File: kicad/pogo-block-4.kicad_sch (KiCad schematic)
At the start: 28 parts, among them J26 VCA_IN, U4 THAT2180, U5 THAT2180, U6 TL072, U63 TL072

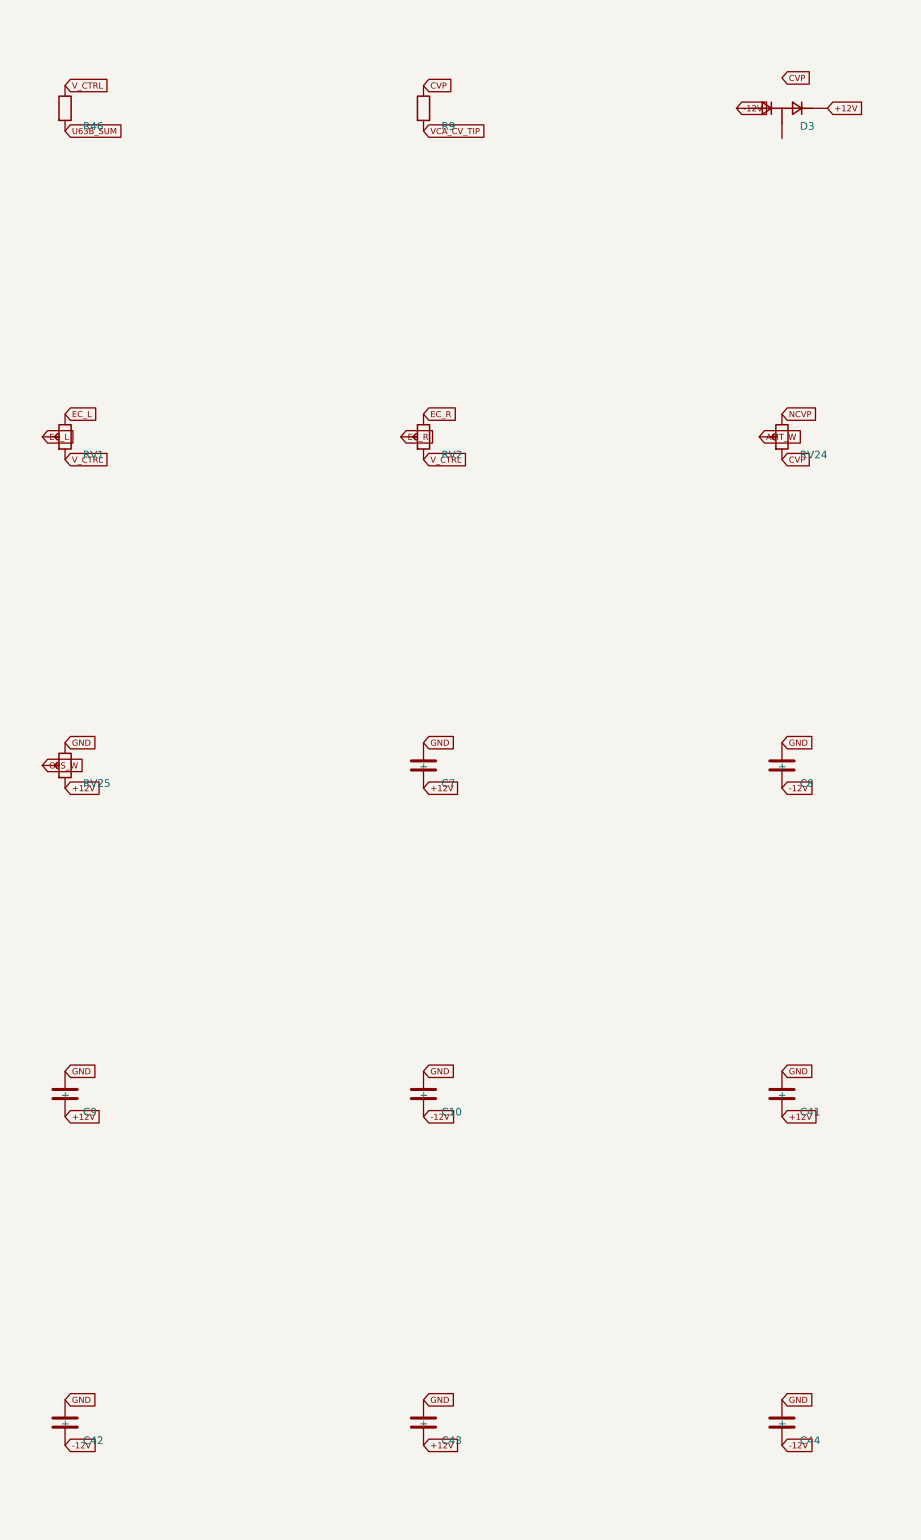
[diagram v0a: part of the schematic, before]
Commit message: 0015-component-audit: apply component verification fixes
Board-breaking:
- that2180: real MPN THAT2180AL08-U (grade A) + package SIP-8 (THT); vendor
  Package_SIP/SIP-8_2.54mm footprint; fix components.yaml U4/U5 + CLAUDE.md.
  The 2180 has no SMD/SOIC variant.
- bat54s: redraw symbol to real series topology (1=A1, 2=K2, 3=K1;A2 junction);
  swap pins 2<->3 on all 24 BAT54S instances (blocks A/1/3/4) so signal sits on the
  junction (pin3), +12V on K2 (pin2), -12V on A1 (pin1); fix aux-cv-protection.md +
  block-A spec (both mislabeled the signal node as pin 2).

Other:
- R_INV_IN/R_INV_FB: add tol 1% (header-required >60 dB null).
- slide_pot_45mm: MPN RA4522F (Alpha 45mm, Rapid/Banzai); fix datasheet link.
- bzx84c10: add shared BZX84_SER datasheet (committed PDF + sha256); canonical MPN.
- opa1612: add symbol opamp2. bourns_3296w/3224w: fix version strings.
- cd4053 symbol doc# -> SCHS047O; c.yaml pin1 '+' -> '~' (non-polarized).

Jack S/T/TN reconciliation deferred (its own change). Plugin DSP untouched.
Regenerated all schematics, BOM, fp-lib-table, footprint SVGs, panel; 5 gates green.
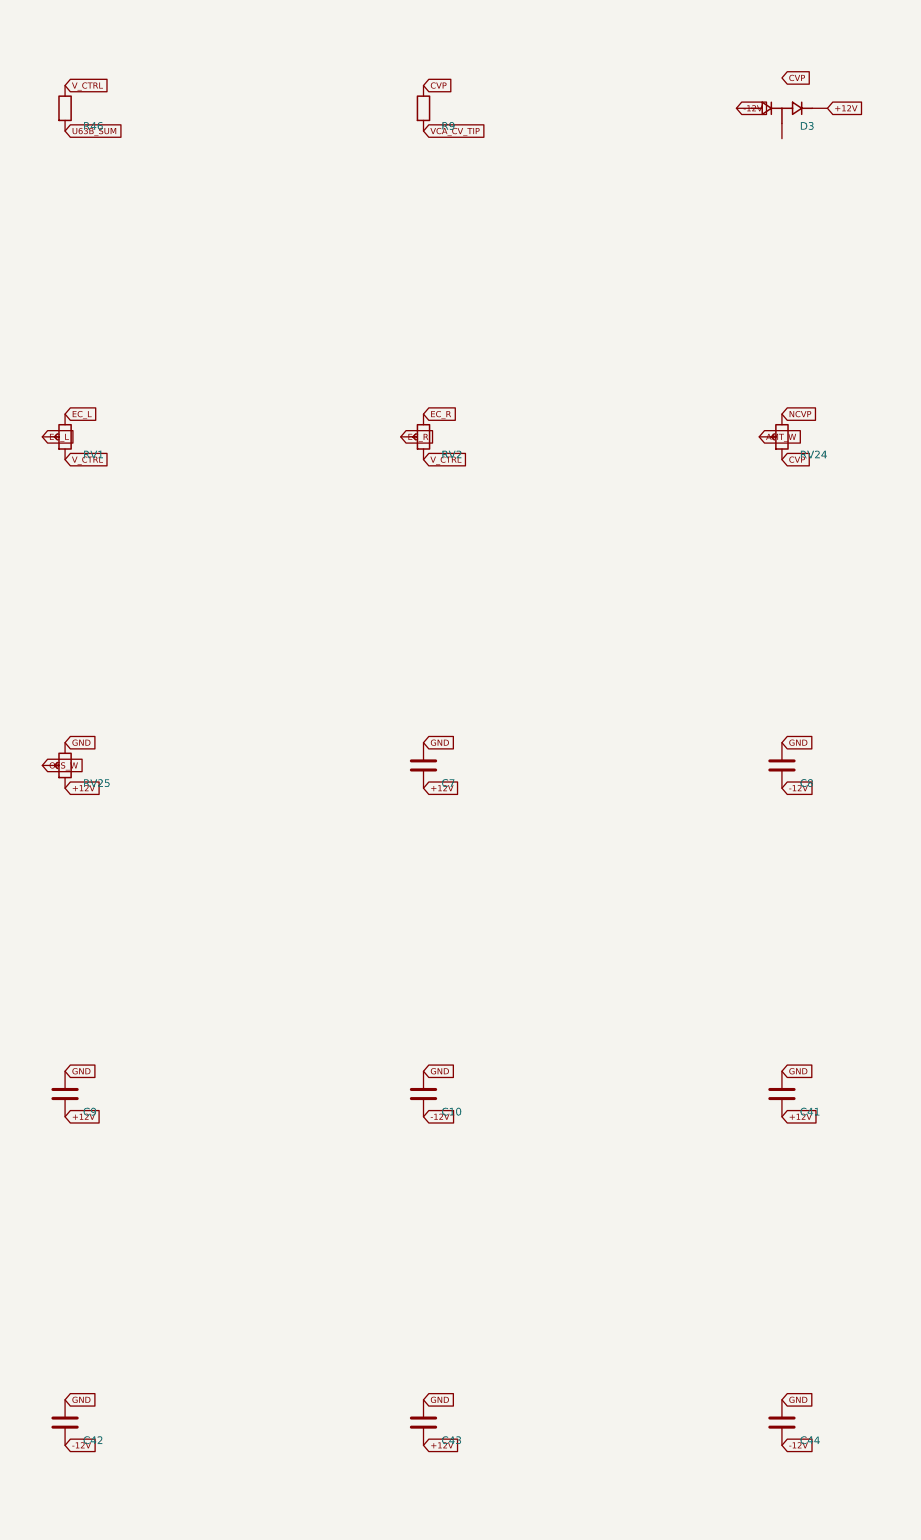
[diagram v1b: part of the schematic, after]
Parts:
- U4, U5: footprint POGO_Package_SO:SOIC-8_3.9x4.9mm_P1.27mm -> POGO_Package_SIP:SIP-8_2.54mm
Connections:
- net +12V: now also D3.2 (K2); no longer D3.3 (K2)
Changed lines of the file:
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@@
   (property "Value" "THAT2180" (at 43.000 39.500 0)
     (effects (font (size 1.016 1.016)) (justify left) (hide yes)))
-  (property "Footprint" "POGO_Package_SO:SOIC-8_3.9x4.9mm_P1.27mm" (at 40.000 40.000 0)
+  (property "Footprint" "POGO_Package_SIP:SIP-8_2.54mm" (at 40.000 40.000 0)
     (effects (font (size 1.016 1.016)) (hide yes)))
 )
@@
   (property "Value" "THAT2180" (at 103.000 39.500 0)
     (effects (font (size 1.016 1.016)) (justify left) (hide yes)))
-  (property "Footprint" "POGO_Package_SO:SOIC-8_3.9x4.9mm_P1.27mm" (at 100.000 40.000 0)
+  (property "Footprint" "POGO_Package_SIP:SIP-8_2.54mm" (at 100.000 40.000 0)
     (effects (font (size 1.016 1.016)) (hide yes)))
 )

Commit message: 0016: source Song Huei R0904N + repoint panel-pot BOM refs (G6a)
- new part components/parts/songhuei_r0904n (matches lin/log/bipolar pot)
- move taper tags off alpha_rd901f (keeps knob/large/xl knob)
- RV41/RV43 (HP_RES/LP2_RES) Bourns 3296W -> R0904N finger pot
- regen block-2/3/4 schematics (att/LFO/VCA pot footprint) + BOM
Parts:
- RV24, RV25: footprint POGO_Potentiometer_THT:Potentiometer_Alpha_RD901F-40-00D_Single_Vertical_CircularHoles -> POGO_Potentiometer_THT:Potentiometer_Songhuei_9mm_TallTrimmer_Vertical
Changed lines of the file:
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@@
   (property "Value" "VCA_AMT" (at 163.000 314.500 0)
     (effects (font (size 1.016 1.016)) (justify left) (hide yes)))
-  (property "Footprint" "POGO_Potentiometer_THT:Potentiometer_Alpha_RD901F-40-00D_Single_Vertical_CircularHoles" (at 160.000 315.000 0)
+  (property "Footprint" "POGO_Potentiometer_THT:Potentiometer_Songhuei_9mm_TallTrimmer_Vertical" (at 160.000 315.000 0)
     (effects (font (size 1.016 1.016)) (hide yes)))
 )
@@
   (property "Value" "VCA_OFS" (at 43.000 369.500 0)
     (effects (font (size 1.016 1.016)) (justify left) (hide yes)))
-  (property "Footprint" "POGO_Potentiometer_THT:Potentiometer_Alpha_RD901F-40-00D_Single_Vertical_CircularHoles" (at 40.000 370.000 0)
+  (property "Footprint" "POGO_Potentiometer_THT:Potentiometer_Songhuei_9mm_TallTrimmer_Vertical" (at 40.000 370.000 0)
     (effects (font (size 1.016 1.016)) (hide yes)))
 )

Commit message: 0018: block-4 ALT-BP VCA cell + OFS placement fix
- ALT-BP VCA (B1 deferral): per the plugin the ALT signal passes through a
  VCA on the SAME control as the main path into BP3 (Pogo.cpp:439-441). Add
  2x THAT2180 (U78 ALT-L, U79 ALT-R) + I/V (U80) + R_in/R_f/Ec+ trims/decoupling,
  all sharing V_ctrl. New boundary nets: ALT_OUT_L/R (in, from block-1) and
  ALT_VCA_OUT_L/R (out, to block-6 BP3 selector). THAT2180 count 2->4.
- VCA_OFS placement fix: the plugin adds OFS to the CV BEFORE the AMT gain law.
  Restructure the CV chain so OFS is summed into the CV ahead of the symmetric
  +/-effCV AMT pot -> AMT=0 (center) gives unity regardless of OFS, matching
  the plugin (old netlist summed OFS after AMT, shifting gain at the detent).
- Renumber VCA pots RV24/RV25 -> RV44/RV45 to clear a base-ref collision with
  block-6's RV24_x/RV25_x expo trims (panel binds by param name, not ref).
- B3 deferral (raw bus normal + VCA_AMT pot in block-4) confirmed already
  satisfied. Refresh aux-vca-cell (4 cells, SIP-8, power, board name, CV chain).

All five --check gates green; parity OK. Block-4 schematic + BOM regenerated.

https://claude.ai/code/session_013jFXG5oeMVSYP7iRpwGvtQ
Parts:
- added C10, C111, C112, C113, C114, C115, C116, C41, C42, C43, C44, C7, C8, C9: 100nF, symbol Device:C
- added J26: VCA_IN, POGO_Connector_Audio:Jack_3.5mm_QingPu_WQP-PJ398SM_Vertical_CircularHoles, symbol Device:Audio_Jack_3.5mm_SwitchT
- added RV46: VCA_UNITY_ALT_L, POGO_Potentiometer_SMD:Potentiometer_Bourns_3224W, symbol Device:R_POT
- added RV47: VCA_UNITY_ALT_R, POGO_Potentiometer_SMD:Potentiometer_Bourns_3224W, symbol Device:R_POT
- D3: renamed from C41; value 100nF -> BAT54S; footprint (none) -> POGO_Package_TO_SOT_SMD:SOT-23; symbol Device:C -> Diode:BAT54S
- R129: renamed from C7; value 100nF -> 20k; symbol Device:C -> Device:R
- R130: renamed from C8; value 100nF -> 20k; symbol Device:C -> Device:R
- R131: renamed from C9; value 100nF -> 20k; symbol Device:C -> Device:R
- R132: renamed from C10; value 100nF -> 20k; symbol Device:C -> Device:R
- R40: renamed from R45; value 100k -> 20k
- R41: renamed from R46; value 2k4 -> 20k
- R42: renamed from R9; value 100R -> 100k
- R43: renamed from D3; value BAT54S -> 100k; footprint POGO_Package_TO_SOT_SMD:SOT-23 -> (none); symbol Diode:BAT54S -> Device:R
- R44: renamed from RV1; value VCA_UNITY_L -> 100k; footprint POGO_Potentiometer_SMD:Potentiometer_Bourns_3224W -> (none); symbol Device:R_POT -> Device:R
- R45: renamed from RV2; value VCA_UNITY_R -> 100k; footprint POGO_Potentiometer_SMD:Potentiometer_Bourns_3224W -> (none); symbol Device:R_POT -> Device:R
- R46: renamed from RV24; value VCA_AMT -> 100k; footprint POGO_Potentiometer_THT:Potentiometer_Songhuei_9mm_TallTrimmer_Vertical -> (none); symbol Device:R_POT -> Device:R
- R7: renamed from R43; value 10k -> 20k
- R8: renamed from R44; value 100k -> 20k
- R9: renamed from RV25; value VCA_OFS -> 100R; footprint POGO_Potentiometer_THT:Potentiometer_Songhuei_9mm_TallTrimmer_Vertical -> (none); symbol Device:R_POT -> Device:R
- RV1: renamed from C42; value 100nF -> VCA_UNITY_L; footprint (none) -> POGO_Potentiometer_SMD:Potentiometer_Bourns_3224W; symbol Device:C -> Device:R_POT
- RV2: renamed from C43; value 100nF -> VCA_UNITY_R; footprint (none) -> POGO_Potentiometer_SMD:Potentiometer_Bourns_3224W; symbol Device:C -> Device:R_POT
- RV44: renamed from C44; value 100nF -> VCA_AMT; footprint (none) -> POGO_Potentiometer_THT:Potentiometer_Songhuei_9mm_TallTrimmer_Vertical; symbol Device:C -> Device:R_POT
- RV45: renamed from J26; value VCA_IN -> VCA_OFS; footprint POGO_Connector_Audio:Jack_3.5mm_QingPu_WQP-PJ398SM_Vertical_CircularHoles -> POGO_Potentiometer_THT:Potentiometer_Songhuei_9mm_TallTrimmer_Vertical; symbol Device:Audio_Jack_3.5mm_SwitchT -> Device:R_POT
- U78: renamed from R7; value 20k -> THAT2180; footprint (none) -> POGO_Package_SIP:SIP-8_2.54mm; symbol Device:R -> POGO:THAT2180
- U79: renamed from R8; value 20k -> THAT2180; footprint (none) -> POGO_Package_SIP:SIP-8_2.54mm; symbol Device:R -> POGO:THAT2180
- U80: renamed from R40; value 20k -> TL072; footprint (none) -> POGO_Package_SO:SOIC-8_3.9x4.9mm_P1.27mm; symbol Device:R -> Amplifier_Operational:OPA1612
- U80: renamed from R41; value 20k -> TL072; symbol Device:R -> Amplifier_Operational:OPA1612
- U80: renamed from R42; value 10k -> TL072; symbol Device:R -> Amplifier_Operational:OPA1612
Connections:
- net +12V: now also RV45.1, U78.5 (V-), U79.5 (V-), U80.4 (V-), C111.2, C113.2, C115.2, C41.2, C43.2, C7.2, C9.2; no longer R129.2, R131.2, R43.2 (K2), R9.1, RV2.2
- net -12V: now also D3.1 (A1), U78.7 (V+), U79.7 (V+), U80.8 (V+), C10.2, C112.2, C114.2, C116.2, C42.2, C44.2, C8.2; no longer R130.2, R132.2, R43.1 (A1), RV1.2, RV44.2
- net CVP: now also R42.2, R9.1; no longer R42.1, R46.1, U80.2
- net EC_L: now also RV1.2 (Wiper), RV1.3; no longer R44.2 (Wiper), R44.3
- net EC_R: now also RV2.2 (Wiper), RV2.3; no longer R45.2 (Wiper), R45.3
- net GND: now also RV45.3, U78.1 (Input), U78.2 (Ec+), U78.3 (Ec-), U79.1 (Input), U79.2 (Ec+), U79.3 (Ec-), U80.2 (In-), U80.6 (In-), C10.1, C111.1, C112.1, C113.1, C114.1, C115.1, C116.1, C41.1, C42.1, C43.1, C44.1, C7.1, C8.1, C9.1, J26.2 (S); no longer D3.1, R129.1, R130.1, R131.1, R132.1, R9.3, RV1.1, RV2.1, RV44.1, RV45.2 (S)
- net IV_L_IN: now also R40.2; no longer U80.2
- net IV_R_IN: now also R41.2; no longer U80.2
- net OFS_W: now also R45.2, RV45.2 (Wiper); no longer R40.2, R9.2 (Wiper)
- net PG_OUT_L: now also R7.2; no longer U78.2
- net PG_OUT_R: now also R8.2; no longer U79.2
- net VCA_CV_TIP: now also R9.2, J26.1 (T); no longer R42.2, RV45.1 (T)
- net VCA_IN_L: now also R7.1; no longer U78.1
- net VCA_IN_R: now also R8.1; no longer U79.1
- net VCA_OUT_L: now also R40.1; no longer U80.1
- net VCA_OUT_R: now also R41.1; no longer U80.1
- net V_CTRL: now also RV1.1, RV2.1, RV44.2 (Wiper), RV46.1, RV47.1; no longer R41.1, R44.1, R45.1, U63.7 (Out)
- net AMT_W renamed U63B_INV
- net U63B_INV: now also R44.1, U63.5 (In+); no longer R8.2
- removed net NCVP: R46.3, R7.1, U63.1 (Out)
- removed net U63A_INV: R7.2, U63.3 (In+), U80.1
- removed net U63B_SUM: R40.1, R41.2, R8.1, U63.5 (In+)
- new net ALT_IV_L_IN: R131.2, U80.3 (In+)
- new net ALT_IV_R_IN: R132.2, U80.5 (In+)
- new net ALT_OUT_L: R129.2
- new net ALT_OUT_R: R130.2
- new net ALT_VCA_IN_L: R129.1, U78.6 (Gnd)
- new net ALT_VCA_IN_R: R130.1, U79.6 (Gnd)
- new net ALT_VCA_OUT_L: R131.1, U80.1 (Out)
- new net ALT_VCA_OUT_R: R132.1, U80.7 (Out)
- new net EC_ALT_L: RV46.2 (Wiper), RV46.3, U78.4 (Sym)
- new net EC_ALT_R: RV47.2 (Wiper), RV47.3, U79.4 (Sym)
- new net NEFFCV: R43.1, R44.2, RV44.3, U63.1 (Out)
- new net PEFFCV: R46.1, RV44.1, U63.7 (Out)
- new net U63A_SUM: R42.1, R43.2, R45.1, U63.3 (In+)
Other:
- moved on the sheet: R40, R41, R42, R7, R8, U80C

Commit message: 0020 HIGH-3: VCA Ec+ injection trims + V_CTRL buffer (10 cells, last cluster)
Replaced the useless series-rheostat-into-high-Z-Ec+ unity trims (~0.004dB
authority) with SPICE-validated voltage-injection trims across all 10 VCA cells:
- block-4 (4 cells: main L/R + ALT L/R): +U97 TL072 buffers the unbuffered AMT
  wiper -> V_CTRL_BUF -> 4x R_ec(10k) -> Ec+ (decouples the cells). Trims RV1/2/46/47
  500ohm->10k as dividers across a shared ±1.2V ref (R233/R234), wiper->R_inj(1M)->Ec+.
- block-6 dist1/2/3 (6 DRIVE cells): same injection trim; V_DRIVE_CTRL_n is already
  an op-amp output (low-Z) so no extra buffer - just per-section ±ref divider + R_ec/R_inj.
  RV51-56 500ohm->10k.
SPICE vca_ecplus_full.cir: g_ctrl 0.984, ±2dB unity authority, nulls bias offset.
New: U97, R233-R260, C117/C118; ~30 parts. All --check gates + JS/Py parity green,
0 schematic FAIL. (Absolute 6.1mV/dB is [NV], absorbed by the ±2dB trim.)

https://claude.ai/code/session_013jFXG5oeMVSYP7iRpwGvtQ
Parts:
- added C10, C111, C112, C113, C114, C115, C116, C41, C42, C43, C44, C7, C8, C9: 100nF, symbol Device:C
- added J26: VCA_IN, POGO_Connector_Audio:Jack_3.5mm_QingPu_WQP-PJ398SM_Vertical_CircularHoles, symbol Device:Audio_Jack_3.5mm_SwitchT
- R233: renamed from C10; value 100nF -> 45k3; symbol Device:C -> Device:R
- R234: renamed from C41; value 100nF -> 45k3; symbol Device:C -> Device:R
- R235: renamed from C42; value 100nF -> 10k; symbol Device:C -> Device:R
- R236: renamed from C43; value 100nF -> 10k; symbol Device:C -> Device:R
- R237: renamed from C44; value 100nF -> 10k; symbol Device:C -> Device:R
- R238: renamed from C111; value 100nF -> 10k; symbol Device:C -> Device:R
- R239: renamed from C112; value 100nF -> 1M; symbol Device:C -> Device:R
- R240: renamed from C113; value 100nF -> 1M; symbol Device:C -> Device:R
- R241: renamed from C114; value 100nF -> 1M; symbol Device:C -> Device:R
- R242: renamed from C115; value 100nF -> 1M; symbol Device:C -> Device:R
- RV46: renamed from C116; value 100nF -> VCA_UNITY_ALT_L; footprint (none) -> POGO_Potentiometer_SMD:Potentiometer_Bourns_3224W; symbol Device:C -> Device:R_POT
- RV47: renamed from J26; value VCA_IN -> VCA_UNITY_ALT_R; footprint POGO_Connector_Audio:Jack_3.5mm_QingPu_WQP-PJ398SM_Vertical_CircularHoles -> POGO_Potentiometer_SMD:Potentiometer_Bourns_3224W; symbol Device:Audio_Jack_3.5mm_SwitchT -> Device:R_POT
- U97: renamed from C7; value 100nF -> TL072; symbol Device:C -> Amplifier_Operational:OPA1612
- U97: renamed from RV46; value VCA_UNITY_ALT_L -> TL072; footprint POGO_Potentiometer_SMD:Potentiometer_Bourns_3224W -> POGO_Package_SO:SOIC-8_3.9x4.9mm_P1.27mm; symbol Device:R_POT -> Amplifier_Operational:OPA1612
- U97: renamed from RV47; value VCA_UNITY_ALT_R -> TL072; footprint POGO_Potentiometer_SMD:Potentiometer_Bourns_3224W -> (none); symbol Device:R_POT -> Amplifier_Operational:OPA1612
- renumbered C8 to C117, C9 to C118
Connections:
- net +12V: now also C117.2, R233.2, U97.4 (V-), C111.2, C113.2, C115.2, C41.2, C43.2, C7.2, C9.2; no longer C118.2, R234.2, R236.2, R238.2, R240.2, R242.2, U97.2
- net -12V: now also C118.2, R234.2, U97.8 (V+), C10.2, C112.2, C114.2, C116.2, C42.2, C44.2, C8.2; no longer C117.2, R233.2, R235.2, R237.2, R239.2, R241.2, RV46.2
- net EC_ALT_L: now also R237.1, R241.1; no longer U97.2 (Wiper), U97.3
- net EC_ALT_R: now also R238.1, R242.1; no longer U97.2 (Wiper), U97.3
- net EC_L: now also R235.1, R239.1; no longer RV1.2 (Wiper), RV1.3
- net EC_R: now also R236.1, R240.1; no longer RV2.2 (Wiper), RV2.3
- net GND: now also U97.6 (In-), C10.1, C111.1, C112.1, C113.1, C114.1, C115.1, C116.1, C41.1, C42.1, C43.1, C44.1, C7.1, C8.1, C9.1, J26.2 (S); no longer R233.1, R234.1, R235.1, R236.1, R237.1, R238.1, R239.1, R240.1, R241.1, R242.1, RV46.1, RV47.2 (S), U97.1
- net VCA_CV_TIP: now also J26.1 (T); no longer RV47.1 (T)
- net V_CTRL: now also U97.2 (In-); no longer RV1.1, RV2.1, U97.1, U97.1
- net REF_P: now reaches RV47.3
- net REF_P: now also R233.1, RV1.3, RV2.3, RV46.3
- new net REF_N: R234.1, RV1.1, RV2.1, RV46.1, RV47.1
- new net TRIMW_ALT_L: R241.2, RV46.2 (Wiper)
- new net TRIMW_ALT_R: R242.2, RV47.2 (Wiper)
- new net TRIMW_L: R239.2, RV1.2 (Wiper)
- new net TRIMW_R: R240.2, RV2.2 (Wiper)
- new net U97B_SPARE: U97.5 (In+), U97.7 (Out)
- new net V_CTRL_BUF: R235.2, R236.2, R237.2, R238.2, U97.1 (Out), U97.3 (In+)
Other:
- moved on the sheet: C117, C118

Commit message: 0025: FIX the HIGH-3 ref-divider bug the SPICE-math gate found (block-4 + block-6)
ref_divider.cir derived REF_P from the actual netlist and got +-0.32V, not the
+-1.2V spec.md:166 + the 0020 HIGH-3 design claimed. Root cause (my error in
0020): R233/R234 sized 45.3k assuming a SINGLE 10k bridge, but all 4 unity trims
(RV1/RV2/RV46/RV47) load REF_P<->REF_N in PARALLEL = 2.5k -> REF_P collapses to
0.32V -> Ec+ injection authority was ~+-0.5dB, not the intended +-2dB. block-6
DRIVE refs had the same bug (2 pots = 5k bridge).

FIX:
- block-4: R233/R234 45k3->11k3 (-> +1.195V at the 2.5k load).
- block-6 dist1/2/3: R243/244/249/250/255/256 45k3->22k6 (-> +1.2V at the 5k load).
- ref_divider deck now pins +1.195V + binds R233=11k3, so a regression to 45k3
  FAILS the gate. Regenerated block-4/dist1/2/3 schematics + BOM.

All 7 --check gates green (incl. SPICE). Second real design error the SPICE-math
methodology has found; first to correct live netlist component values.

https://claude.ai/code/session_013jFXG5oeMVSYP7iRpwGvtQ
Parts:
- R233, R234: value 45k3 -> 11k3
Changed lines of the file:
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@@
   (property "Reference" "R233" (at 163.000 538.000 0)
     (effects (font (size 1.27 1.27)) (justify left)))
-  (property "Value" "45k3" (at 163.000 534.500 0)
+  (property "Value" "11k3" (at 163.000 534.500 0)
     (effects (font (size 1.016 1.016)) (justify left) (hide yes)))
 )
@@
   (property "Reference" "R234" (at 43.000 593.000 0)
     (effects (font (size 1.27 1.27)) (justify left)))
-  (property "Value" "45k3" (at 43.000 589.500 0)
+  (property "Value" "11k3" (at 43.000 589.500 0)
     (effects (font (size 1.016 1.016)) (justify left) (hide yes)))
 )
